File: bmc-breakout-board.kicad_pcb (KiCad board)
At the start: 4 copper layers, 90 x 60 mm, 26 parts, among them J1 PinHeader_2x4, J10 PinHeader_2x4, J11 PinHeader_2x05, J12 61300411121, J14 PCIE_BUS_x1, J15 0473460001, J16 PinHeader_1x07, J17 UE27AC54100, J2 PinHeader_2x13, J3 PinHeader_2x08, J4 61300411121, J5 ME1016813401101, J6 61300411121, J7 DC_SOCKET, J8 PinHeader_2x05, J9 PinHeader_1x07, Q1 BSS138AKA

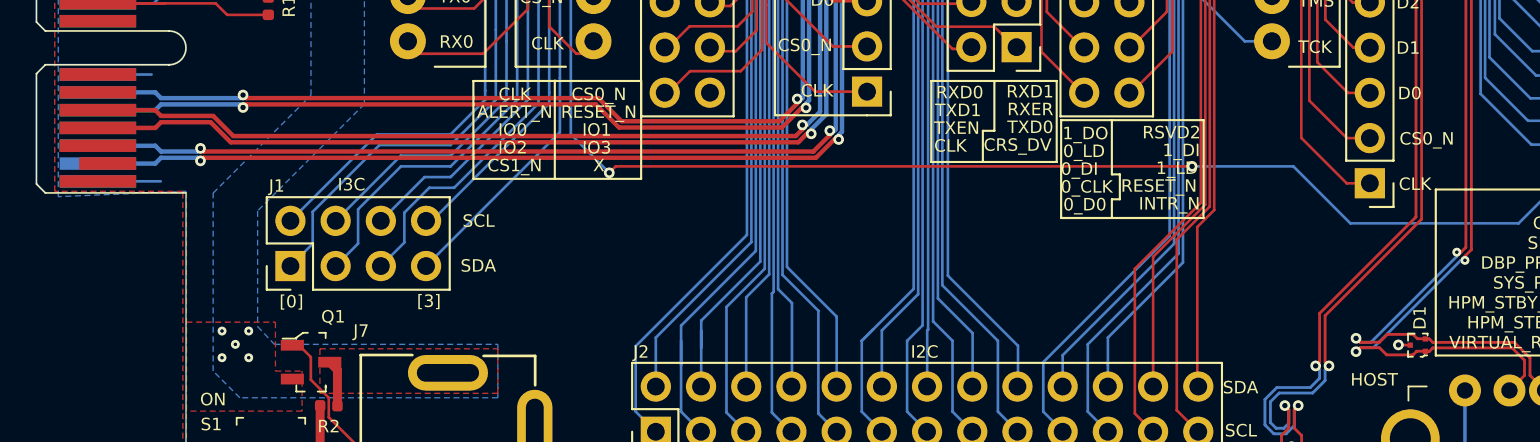
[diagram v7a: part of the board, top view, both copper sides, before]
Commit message: Add decoupling on PCIe lines
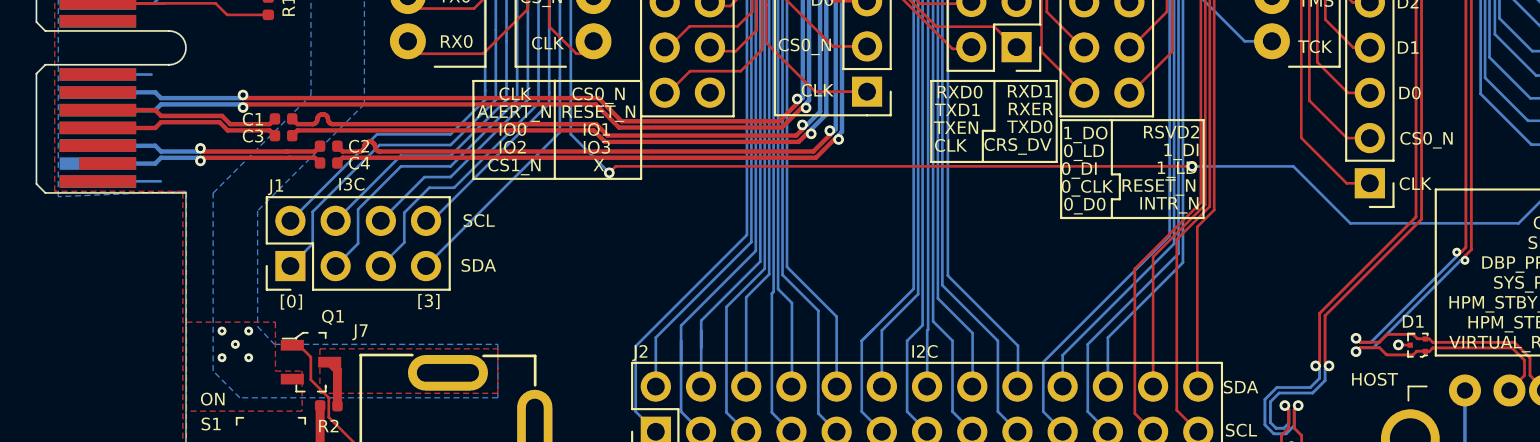
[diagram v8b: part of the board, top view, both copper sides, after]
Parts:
- added C1: C_100n_0402, bmc-breakout-board-footprints:0402-cap, F.Cu at (65.6, 95.0)
- added C2: C_100n_0402, bmc-breakout-board-footprints:0402-cap, F.Cu at (68.1, 96.5)
- added C3: C_100n_0402, bmc-breakout-board-footprints:0402-cap, F.Cu at (65.6, 95.9)
- added C4: C_100n_0402, bmc-breakout-board-footprints:0402-cap, F.Cu at (68.1, 97.5)
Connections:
- J5 pad A15: PCIE_BMC_TX_P -> /TX_P
- J5 pad A16: PCIE_BMC_TX_N -> /TX_N
- J5 pad A18: PCIE_BMC_RX_P -> /RX_P
- J5 pad A19: PCIE_BMC_RX_N -> /RX_N
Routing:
- net PCIE_BMC_TX_N: track 72.3 -> 10.4 mm, vias 1 -> 0
- net PCIE_BMC_TX_P: track 71.8 -> 10.4 mm, vias 1 -> 0
- net /TX_P: track 0.00 -> 61.2 mm, vias 0 -> 1
- net /TX_N: track 0.00 -> 61.2 mm, vias 0 -> 1
- net PCIE_BMC_RX_N: track 73.8 -> 12.9 mm, vias 2 -> 1
- net PCIE_BMC_RX_P: track 73.2 -> 12.9 mm, vias 2 -> 1
- net /RX_P: track 0.00 -> 60.2 mm, vias 0 -> 1
- net /RX_N: track 0.00 -> 60.2 mm, vias 0 -> 1
